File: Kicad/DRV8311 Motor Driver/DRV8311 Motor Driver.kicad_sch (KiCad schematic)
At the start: 29 parts, among them J1 1.27mm pin header, J10 Keystone 3569, J11 Keystone 3579, J2 1.27mm pin header, J3 Keystone 3579, J4 Molex Picoblade, J5 Keystone 3569, J6 Keystone 3569, J7 Keystone 3579, J8 Keystone 3569, J9 Keystone 3579, U1 DRV8311HRRWR

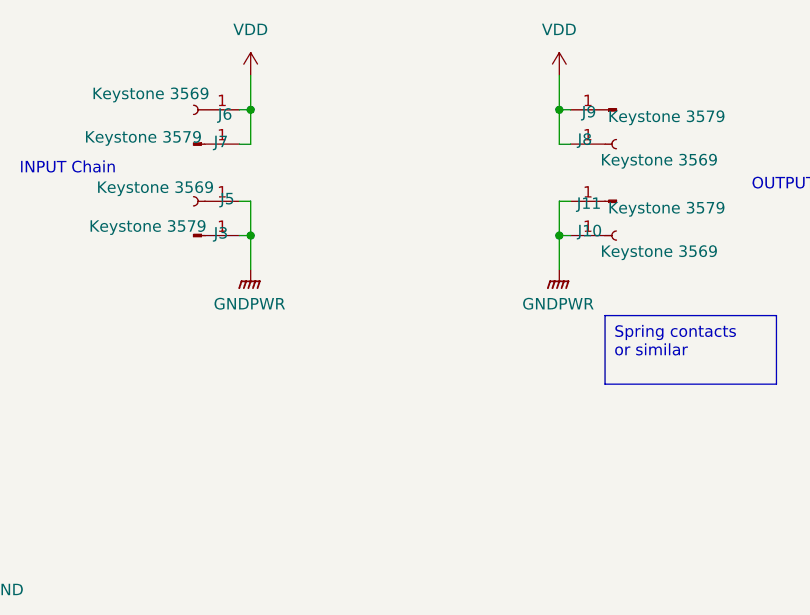
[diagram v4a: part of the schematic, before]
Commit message: Updated 3D models and exported 3D model for DRV8311 board
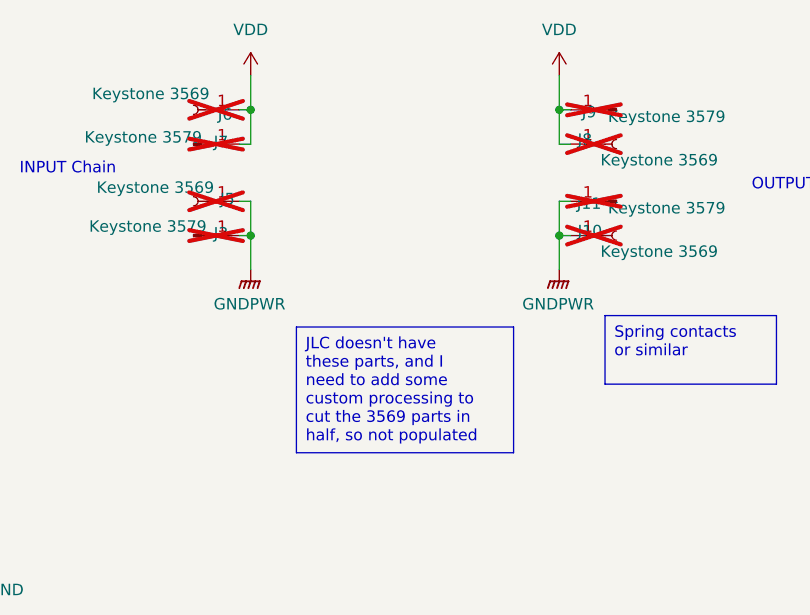
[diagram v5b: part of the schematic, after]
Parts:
- J10, J5, J6, J8: footprint custom_Connector:Keystone_3569 -> custom_Connector:Keystone_3569_half; now not fitted
- J11, J3, J7, J9: now not fitted
- TP3, TP4, TP5: now left out of the parts list
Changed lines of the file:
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@@
 		)
 	)
+	(text_box "JLC doesn't have these parts, and I need to add some custom processing to cut the 3569 parts in half, so not populated"
+		(exclude_from_sim no)
+		(at 220.98 53.34 0)
+		(size 24.13 13.97)
+		(stroke
+			(width 0)
+			(type default)
+		)
+		(fill
+			(type none)
+		)
+		(effects
+			(font
+				(size 1.27 1.27)
+			)
+			(justify left top)
+		)
+	)
 	(text_box "Any capacitors on the power supply line should be rated above my intended voltage range of 3.7-7.4v\nThe bulk capacitance on VM should also be really high"
 		(exclude_from_sim no)
@@
 		(in_bom yes)
 		(on_board yes)
-		(dnp no)
+		(dnp yes)
 		(property "Reference" "J7"
 			(at 212.598 32.766 0)
@@
 		(unit 1)
 		(exclude_from_sim no)
-		(in_bom yes)
+		(in_bom no)
 		(on_board yes)
 		(dnp no)
@@
 		(in_bom yes)
 		(on_board yes)
-		(dnp no)
+		(dnp yes)
 		(property "Reference" "J9"
 			(at 253.492 29.464 0)
@@
 		(in_bom yes)
 		(on_board yes)
-		(dnp no)
+		(dnp yes)
 		(property "Reference" "J3"
 			(at 212.598 42.926 0)
@@
 		(in_bom yes)
 		(on_board yes)
-		(dnp no)
+		(dnp yes)
 		(property "Reference" "J6"
 			(at 213.868 29.718 0)
@@
 			)
 		)
-		(property "Footprint" "custom_Connector:Keystone_3569"
+		(property "Footprint" "custom_Connector:Keystone_3569_half"
 			(at 209.55 29.21 0)
 			(effects
@@
 		(in_bom yes)
 		(on_board yes)
-		(dnp no)
+		(dnp yes)
 		(property "Reference" "J11"
 			(at 253.492 39.624 0)
@@
 		(in_bom yes)
 		(on_board yes)
-		(dnp no)
+		(dnp yes)
 		(property "Reference" "J5"
 			(at 214.122 39.116 0)
@@
 			)
 		)
-		(property "Footprint" "custom_Connector:Keystone_3569"
+		(property "Footprint" "custom_Connector:Keystone_3569_half"
 			(at 209.55 39.37 0)
 			(effects
@@
 		(unit 1)
 		(exclude_from_sim no)
-		(in_bom yes)
+		(in_bom no)
 		(on_board yes)
 		(dnp no)
@@
 		(in_bom yes)
 		(on_board yes)
-		(dnp no)
+		(dnp yes)
 		(property "Reference" "J10"
 			(at 252.222 42.672 0)
@@
 			)
 		)
-		(property "Footprint" "custom_Connector:Keystone_3569"
+		(property "Footprint" "custom_Connector:Keystone_3569_half"
 			(at 256.54 43.18 0)
 			(effects
@@
 		(unit 1)
 		(exclude_from_sim no)
-		(in_bom yes)
+		(in_bom no)
 		(on_board yes)
 		(dnp no)
@@
 		(in_bom yes)
 		(on_board yes)
-		(dnp no)
+		(dnp yes)
 		(property "Reference" "J8"
 			(at 252.222 32.512 0)
@@
 			)
 		)
-		(property "Footprint" "custom_Connector:Keystone_3569"
+		(property "Footprint" "custom_Connector:Keystone_3569_half"
 			(at 256.54 33.02 0)
 			(effects

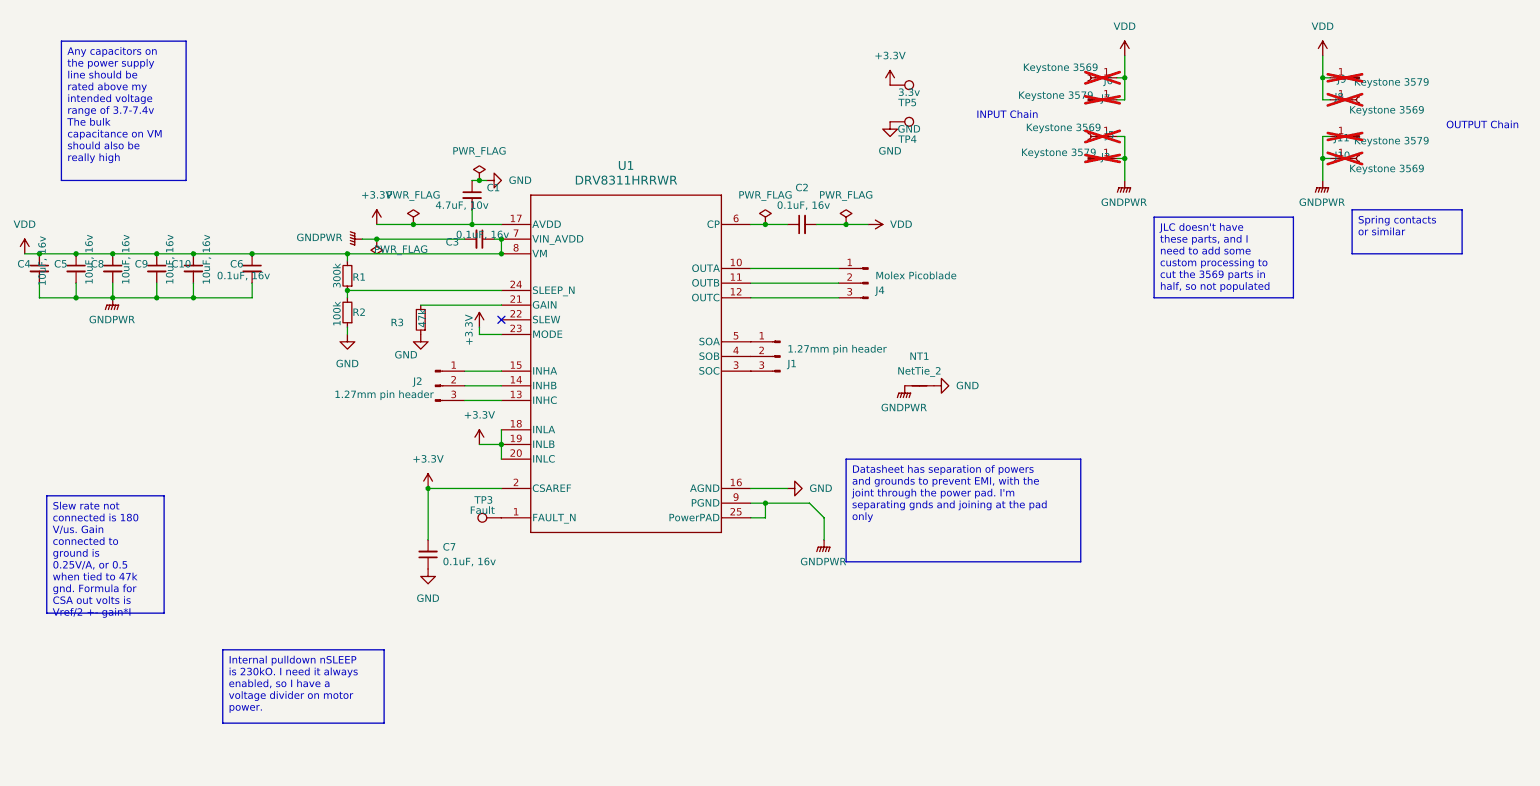
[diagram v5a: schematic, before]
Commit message: Added LCSC part numbers, DNP attr, and exported Gerbers
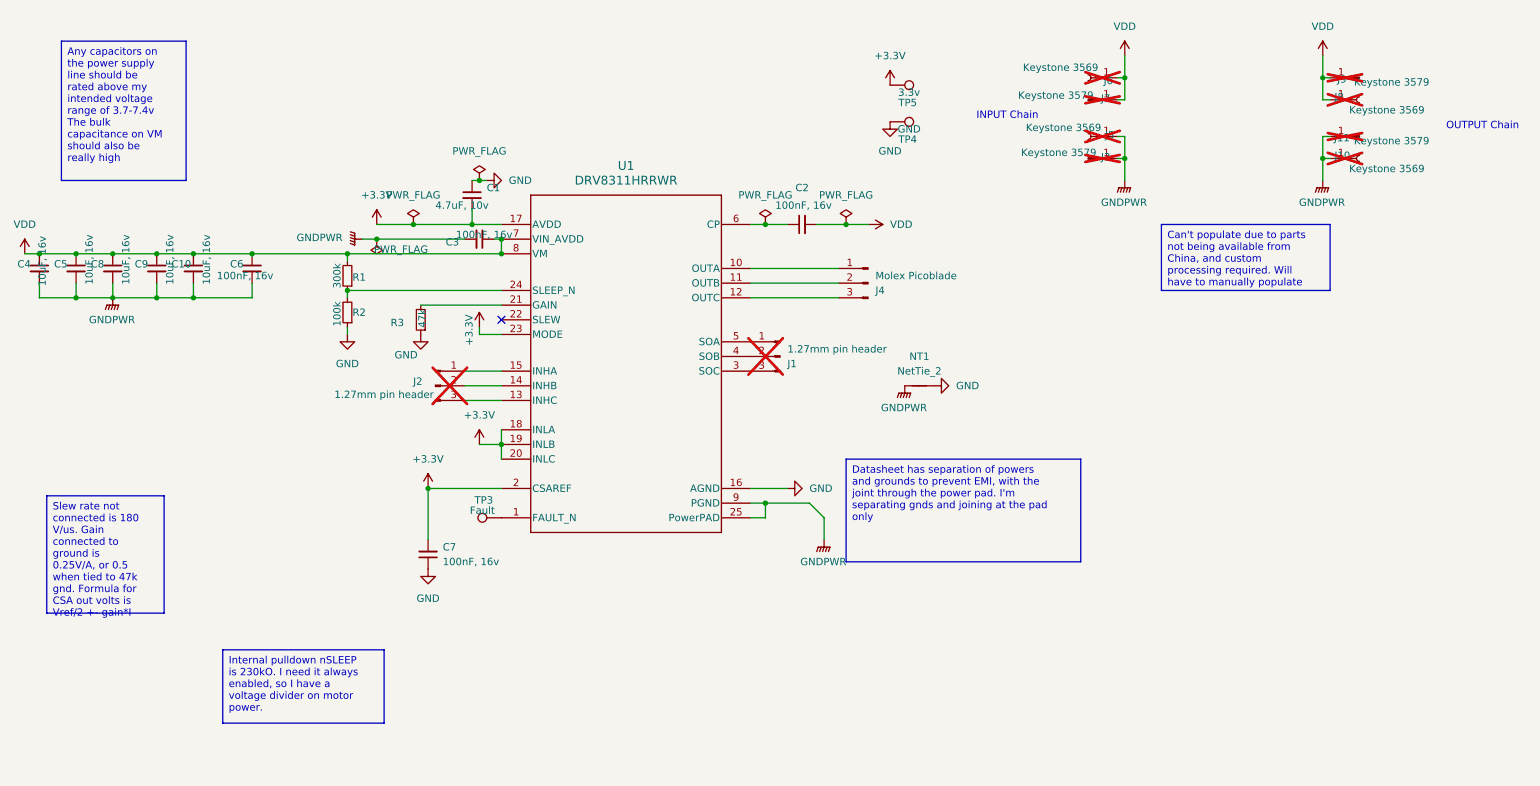
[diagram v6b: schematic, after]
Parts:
- C2, C3, C6, C7: value 0.1uF, 16v -> 100nF, 16v
- J1, J2: now not fitted
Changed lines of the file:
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@@
 		)
 	)
-	(text_box "Spring contacts or similar"
-		(exclude_from_sim no)
-		(at 255.27 52.07 0)
-		(size 19.05 7.62)
+	(text_box "Can't populate due to parts not being available from China, and custom processing required. Will have to manually populate"
+		(exclude_from_sim no)
+		(at 222.25 54.61 0)
+		(size 29.21 11.43)
 		(stroke
 			(width 0)
@@
 		)
 	)
-	(text_box "JLC doesn't have these parts, and I need to add some custom processing to cut the 3569 parts in half, so not populated"
-		(exclude_from_sim no)
-		(at 220.98 53.34 0)
-		(size 24.13 13.97)
-		(stroke
-			(width 0)
-			(type default)
-		)
-		(fill
-			(type none)
-		)
-		(effects
-			(font
-				(size 1.27 1.27)
-			)
-			(justify left top)
-		)
-	)
 	(text_box "Any capacitors on the power supply line should be rated above my intended voltage range of 3.7-7.4v\nThe bulk capacitance on VM should also be really high"
 		(exclude_from_sim no)
@@
 			)
 		)
-		(property "Value" "0.1uF, 16v"
+		(property "Value" "100nF, 16v"
 			(at 97.79 113.0235 0)
 			(effects
@@
 		(in_bom yes)
 		(on_board yes)
-		(dnp no)
+		(dnp yes)
 		(property "Reference" "J1"
 			(at 157.48 78.7401 0)
@@
 			)
 		)
-		(property "Value" "0.1uF, 16v"
+		(property "Value" "100nF, 16v"
 			(at 100.076 56.388 90)
 			(effects
@@
 		(in_bom yes)
 		(on_board yes)
-		(dnp no)
+		(dnp yes)
 		(property "Reference" "J2"
 			(at 93.472 81.788 0)
@@
 			)
 		)
-		(property "Value" "0.1uF, 16v"
+		(property "Value" "100nF, 16v"
 			(at 160.274 51.308 90)
 			(effects
@@
 			)
 		)
-		(property "Value" "0.1uF, 16v"
+		(property "Value" "100nF, 16v"
 			(at 58.674 63.5 0)
 			(effects
